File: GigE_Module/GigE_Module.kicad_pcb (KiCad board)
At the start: 2 copper layers, 33.5 x 25.2 mm, 25 parts, among them J1 Conn_01x10_Socket, J2 Conn_01x10_Socket, J3 RJ45_LED, U4 ENC28J60x-SS, Y1 25MHz

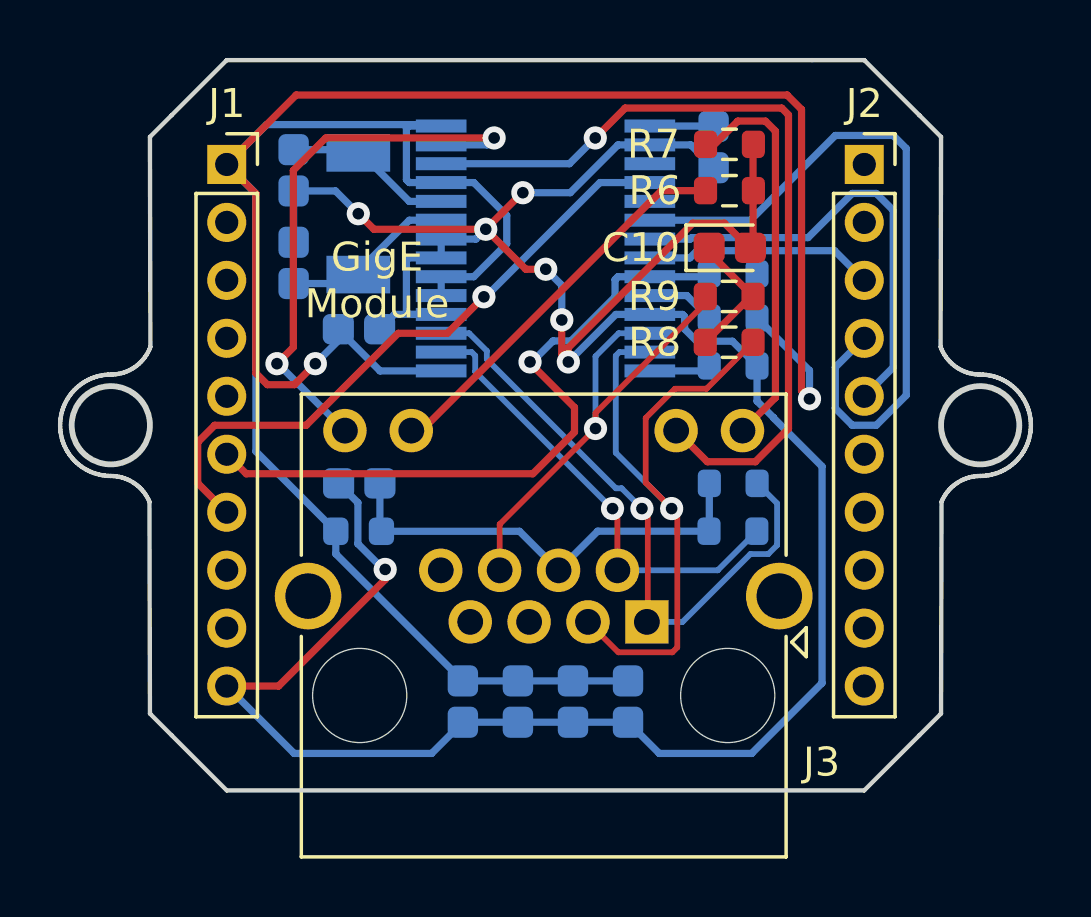
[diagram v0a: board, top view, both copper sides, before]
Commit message: Adding label pins in each PCB design
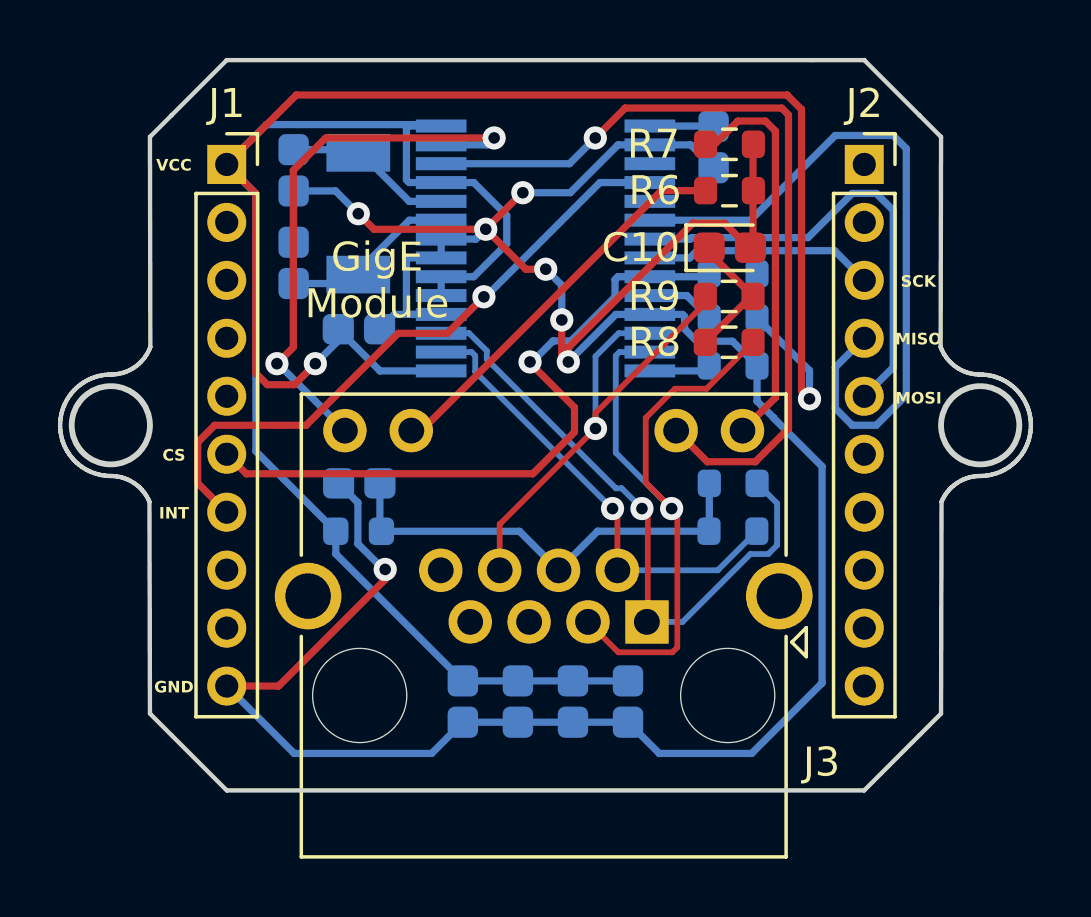
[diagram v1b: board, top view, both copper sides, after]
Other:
- board text added: "CS"
- board text added: "GND"
- board text added: "INT"
- board text added: "MISO"
- board text added: "MOSI"
- board text added: "SCK"
- board text added: "VCC"
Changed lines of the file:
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@@
   (gr_line (start 130.836884 97.245172) (end 130.901863 97.321157)
     (stroke (width 0.15) (type solid)) (layer "Edge.Cuts"))
+  (gr_text "GND" (at 131.95 104.06) (layer "F.SilkS")
+    (effects (font (size 0.4 0.4) (thickness 0.1) bold))
+  )
+  (gr_text "INT" (at 131.95 98.06) (layer "F.SilkS")
+    (effects (font (size 0.4 0.4) (thickness 0.1) bold))
+  )
+  (gr_text "SCK" (at 157.64 90.06) (layer "F.SilkS")
+    (effects (font (size 0.4 0.4) (thickness 0.1) bold))
+  )
   (gr_text "GigE\nModule" (at 138.96 90.03) (layer "F.SilkS")
     (effects (font (size 1 1) (thickness 0.15)))
   )
+  (gr_text "CS" (at 131.95 96.06) (layer "F.SilkS")
+    (effects (font (size 0.4 0.4) (thickness 0.1) bold))
+  )
+  (gr_text "VCC" (at 131.95 86.05) (layer "F.SilkS")
+    (effects (font (size 0.4 0.4) (thickness 0.1) bold))
+  )
+  (gr_text "MISO" (at 157.64 92.05) (layer "F.SilkS")
+    (effects (font (size 0.4 0.4) (thickness 0.1) bold))
+  )
+  (gr_text "MOSI" (at 157.64 94.09) (layer "F.SilkS")
+    (effects (font (size 0.4 0.4) (thickness 0.1) bold))
+  )
   (gr_text "BTN" (at 151.772 81.725 -165) (layer "Eco1.User")

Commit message: Adding FPV 4-pin interface module
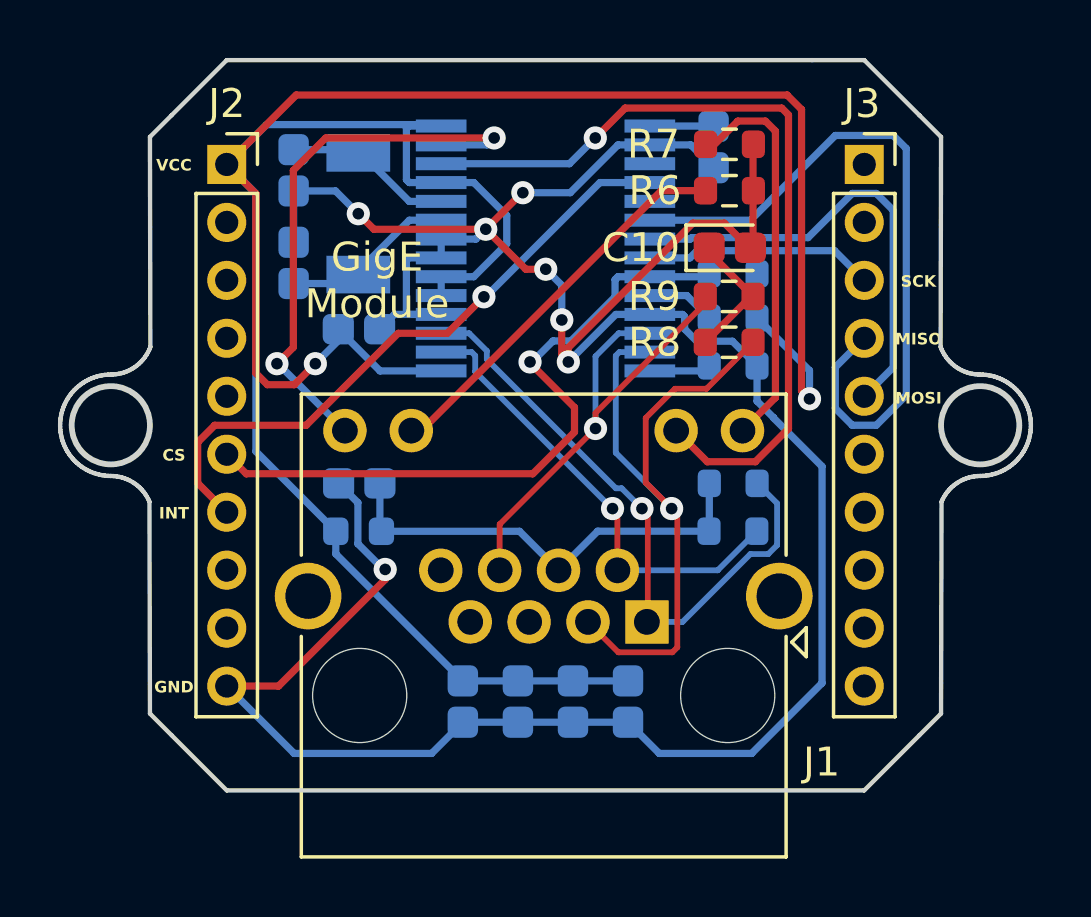
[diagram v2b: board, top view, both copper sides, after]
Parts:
- renumbered J3 to J1, J1 to J2, J2 to J3
